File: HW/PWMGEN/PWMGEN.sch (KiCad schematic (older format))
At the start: 28 parts, among them Q1 MMBT3904, U2 MCP1825ST-3302E/DB, U3 uA78M05C, U4 STM32L011D4Px, U5 LM4132AMF-3.3

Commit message: updated layout
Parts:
- R7: footprint Resistor_SMD:R_1206_3216Metric_Pad1.42x1.75mm_HandSolder -> Resistor_THT:R_Axial_DIN0207_L6.3mm_D2.5mm_P7.62mm_Horizontal
- U2, U3: symbol Regulator_Linear:LM78M05_TO220 -> PWMGEN-rescue:LM78M05_TO220-Regulator_Linear
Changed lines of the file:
@@
 	7600 3650 7600 3850
 $Comp
-L Regulator_Linear:LM78M05_TO220 U2
+L PWMGEN-rescue:LM78M05_TO220-Regulator_Linear U2
 U 1 1 5D9A22DE
 P 4300 1750
@@
 $EndComp
 $Comp
-L Regulator_Linear:LM78M05_TO220 U3
+L PWMGEN-rescue:LM78M05_TO220-Regulator_Linear U3
 U 1 1 5D9A33C6
 P 2800 1750
@@
 F 0 "R7" V 3850 6150 50  0000 L CNN
 F 1 "5K6" V 4050 6150 50  0000 L CNN
-F 2 "Resistor_SMD:R_1206_3216Metric_Pad1.42x1.75mm_HandSolder" V 3880 6200 50  0001 C CNN
+F 2 "Resistor_THT:R_Axial_DIN0207_L6.3mm_D2.5mm_P7.62mm_Horizontal" V 3880 6200 50  0001 C CNN
 F 3 "~" H 3950 6200 50  0001 C CNN
 	1    3950 6200

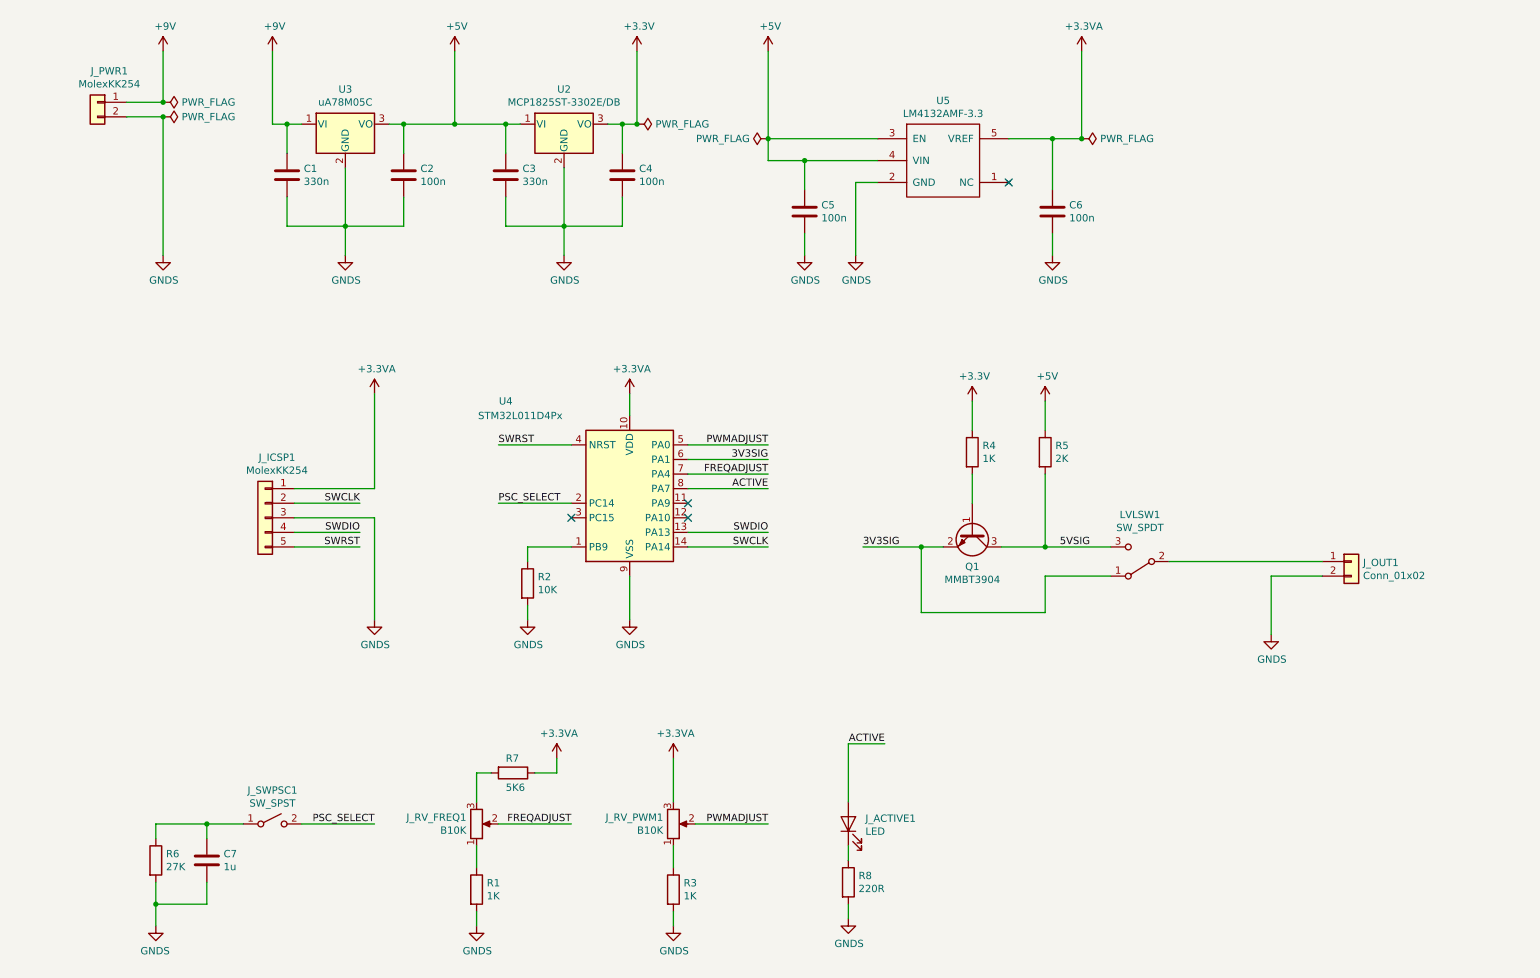
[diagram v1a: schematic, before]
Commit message: updated MCU, layout, sw
- Changed from STM32L011D4 to STM32F051K8
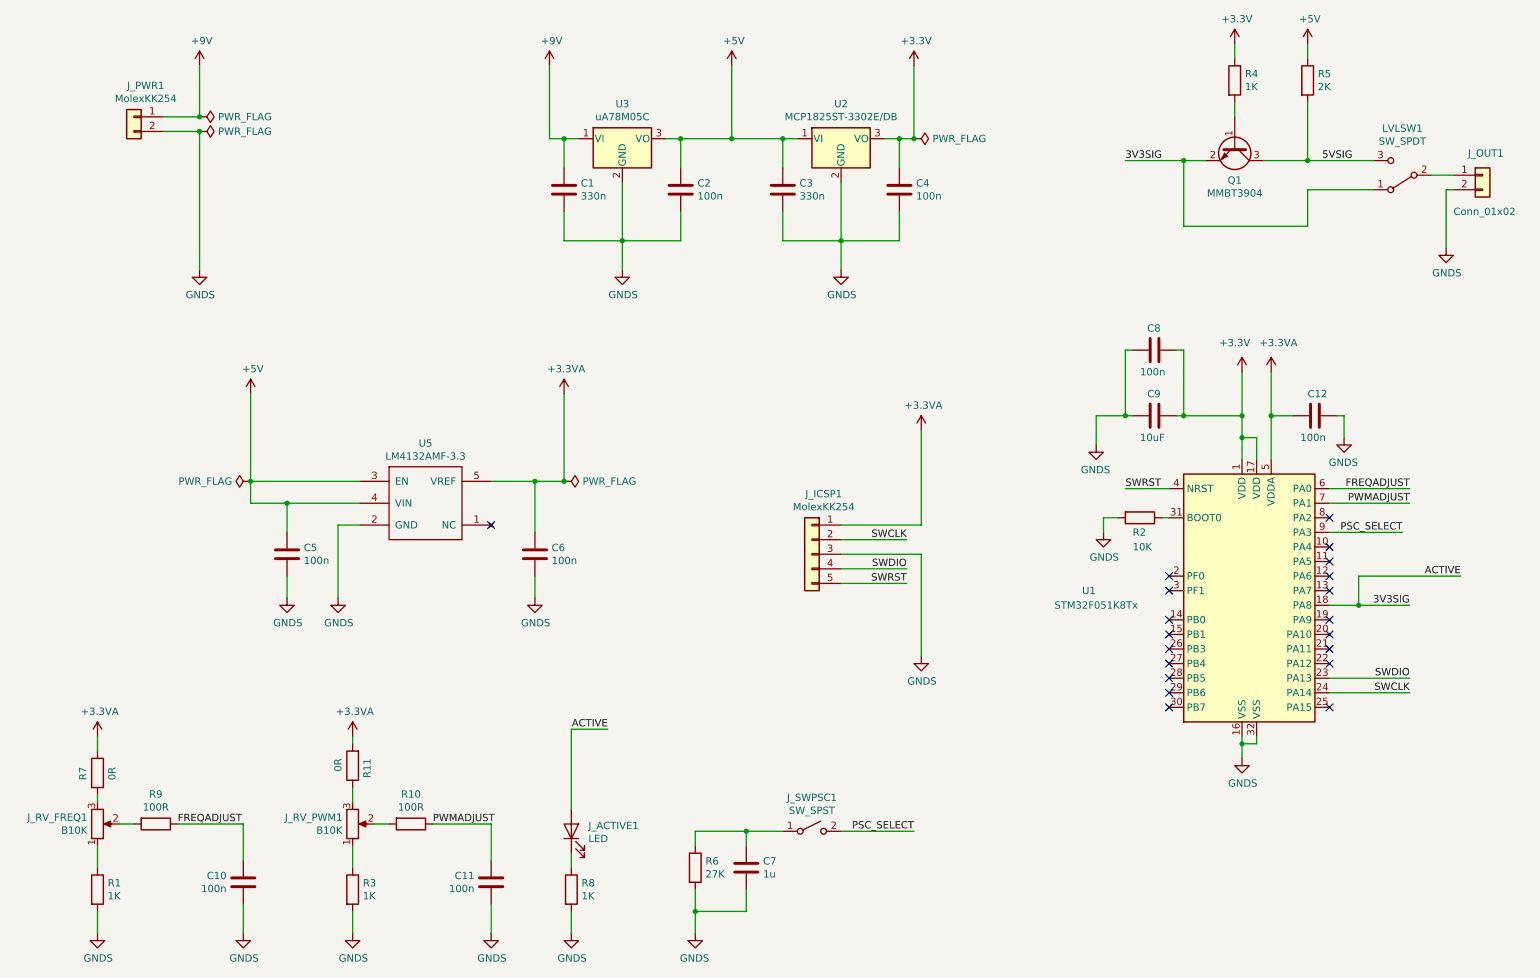
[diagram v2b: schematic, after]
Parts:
- removed U4: STM32L011D4Px, Package_SO:TSSOP-14_4.4x5mm_P0.65mm, symbol MCU_ST_STM32L0:STM32L011D4Px
- added C10, C11, C12, C8: 100n, Capacitor_SMD:C_1206_3216Metric_Pad1.42x1.75mm_HandSolder, symbol Device:C
- added C9: 10uF, Capacitor_SMD:C_1206_3216Metric_Pad1.42x1.75mm_HandSolder, symbol Device:C
- added R10, R9: 100R, Resistor_SMD:R_1206_3216Metric_Pad1.42x1.75mm_HandSolder, symbol Device:R
- added R11: 0R, Resistor_SMD:R_1206_3216Metric_Pad1.42x1.75mm_HandSolder, symbol Device:R
- added U1: STM32F051K8Tx, Package_QFP:LQFP-32_7x7mm_P0.8mm, symbol MCU_ST_STM32F0:STM32F051K8Tx
- J_SWPSC1: footprint Connector_PinHeader_2.54mm:PinHeader_1x03_P2.54mm_Vertical -> Connector_PinHeader_2.54mm:PinHeader_1x02_P2.54mm_Vertical
- R7: value 5K6 -> 0R; footprint Resistor_THT:R_Axial_DIN0207_L6.3mm_D2.5mm_P7.62mm_Horizontal -> Resistor_SMD:R_1206_3216Metric_Pad1.42x1.75mm_HandSolder
- R8: value 220R -> 1K
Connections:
- net ACTIVE is gone; now on net 3V3SIG: J_ACTIVE1.2 (A)
- net +3.3VA: now also C12.2, R11.2, U1.5 (VDDA); no longer J_RV_PWM1.3
- net +3V3: now also C8.1, C9.1, U1.1 (VDD), U1.17 (VDD)
- net 3V3SIG: now also U1.18 (PA8)
- net FREQADJUST: now also C10.1, R9.1, U1.6 (PA0); no longer J_RV_FREQ1.2
- net GNDS: now also C10.2, C11.2, C12.1, C8.2, C9.2, U1.16 (VSS), U1.32 (VSS)
- net PSC_SELECT: now also U1.9 (PA3)
- net PWMADJUST: now also C11.1, R10.1, U1.7 (PA1); no longer J_RV_PWM1.2
- net SWCLK: now also U1.24 (PA14)
- net SWDIO: now also U1.23 (PA13)
- net SWRST: now also U1.4 (NRST)
- net at R2.1: now also U1.31 (BOOT0)
- new net: J_RV_PWM1.2, R10.2
- new net: J_RV_PWM1.3, R11.1
- new net: J_RV_FREQ1.2, R9.2
- no-connect marks 4 -> 20
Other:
- moved on the sheet: C1, C2, C3, C4, C5, C6, C7, J_ACTIVE1, J_ICSP1, J_OUT1, J_PWR1, J_RV_FREQ1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

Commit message: UPDATES
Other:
- note added: "CURRENT\nLIMITER"
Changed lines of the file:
@@
 Wire Wire Line
 	1100 6350 1100 6400
+Text Notes 700  7050 0    50   ~ 0
+CURRENT\nLIMITER
 $EndSCHEMATC

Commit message: UPDATES
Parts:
- removed C10, C11: 100n, Capacitor_SMD:C_1206_3216Metric_Pad1.42x1.75mm_HandSolder, symbol Device:C
- removed R10: 100R, Resistor_SMD:R_1206_3216Metric_Pad1.42x1.75mm_HandSolder, symbol Device:R
- R1: value 1K -> 2k
- R3: value 1K -> 0R
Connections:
- net FREQADJUST: now also J_RV_FREQ1.2; no longer R9.1
- net PWMADJUST: now also J_RV_PWM1.2
- net at R9.2: now also LVLSW1.2 (B); no longer J_RV_FREQ1.2
- net at J_OUT1.1 (Pin_1): now also R9.1; no longer LVLSW1.2 (B)
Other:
- moved on the sheet: LVLSW1, Q1, R4, R5
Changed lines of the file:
@@
 P 2850 7000
 F 0 "R3" H 2920 7045 50  0000 L CNN
-F 1 "1K" H 2920 6956 50  0000 L CNN
+F 1 "0R" H 2920 6956 50  0000 L CNN
 F 2 "Resistor_SMD:R_1206_3216Metric_Pad1.42x1.75mm_HandSolder" V 2780 7000 50  0001 C CNN
 F 3 "~" H 2850 7000 50  0001 C CNN
@@
 	1    0    0    -1
 $EndComp
-Text Label 3400 6550 0    50   ~ 0
+Text Label 3550 6550 2    50   ~ 0
 PWMADJUST
 $Comp
@@
 P 1100 7000
 F 0 "R1" H 1170 7045 50  0000 L CNN
-F 1 "1K" H 1170 6956 50  0000 L CNN
+F 1 "2k" H 1170 6956 50  0000 L CNN
 F 2 "Resistor_SMD:R_1206_3216Metric_Pad1.42x1.75mm_HandSolder" V 1030 7000 50  0001 C CNN
 F 3 "~" H 1100 7000 50  0001 C CNN
@@
 	1    0    0    -1
 $EndComp
-Wire Wire Line
-	1250 6550 1350 6550
-Text Label 1650 6550 0    50   ~ 0
+Text Label 1800 6550 2    50   ~ 0
 FREQADJUST
 Wire Wire Line
@@
 L Transistor_BJT:MMBT3904 Q1
 U 1 1 5D98DE38
-P 8900 1900
-F 0 "Q1" V 9135 1900 50  0000 C CNN
-F 1 "MMBT3904" V 9224 1900 50  0000 C CNN
-F 2 "Package_TO_SOT_SMD:SOT-23" H 9100 1825 50  0001 L CIN
-F 3 "https://docs-emea.rs-online.com/webdocs/1276/0900766b81276adc.pdf" H 8900 1900 50  0001 L CNN
-	1    8900 1900
+P 8550 1900
+F 0 "Q1" V 8785 1900 50  0000 C CNN
+F 1 "MMBT3904" V 8874 1900 50  0000 C CNN
+F 2 "Package_TO_SOT_SMD:SOT-23" H 8750 1825 50  0001 L CIN
+F 3 "https://docs-emea.rs-online.com/webdocs/1276/0900766b81276adc.pdf" H 8550 1900 50  0001 L CNN
+	1    8550 1900
 	0    1    1    0
 $EndComp
@@
 L Device:R R4
 U 1 1 5D98FAB4
-P 8900 1450
-F 0 "R4" H 8970 1495 50  0000 L CNN
-F 1 "1K" H 8970 1406 50  0000 L CNN
-F 2 "Resistor_SMD:R_1206_3216Metric_Pad1.42x1.75mm_HandSolder" V 8830 1450 50  0001 C CNN
-F 3 "~" H 8900 1450 50  0001 C CNN
-	1    8900 1450
+P 8550 1450
+F 0 "R4" H 8620 1495 50  0000 L CNN
+F 1 "1K" H 8620 1406 50  0000 L CNN
+F 2 "Resistor_SMD:R_1206_3216Metric_Pad1.42x1.75mm_HandSolder" V 8480 1450 50  0001 C CNN
+F 3 "~" H 8550 1450 50  0001 C CNN
+	1    8550 1450
 	1    0    0    -1
 $EndComp
@@
 L Device:R R5
 U 1 1 5D98FCF4
-P 9400 1450
-F 0 "R5" H 9470 1495 50  0000 L CNN
-F 1 "2K" H 9470 1406 50  0000 L CNN
-F 2 "Resistor_SMD:R_1206_3216Metric_Pad1.42x1.75mm_HandSolder" V 9330 1450 50  0001 C CNN
-F 3 "~" H 9400 1450 50  0001 C CNN
-	1    9400 1450
-	1    0    0    -1
-$EndComp
-Wire Wire Line
-	9100 2000 9400 2000
-Wire Wire Line
-	9400 2000 9400 1600
-Wire Wire Line
-	8900 1600 8900 1700
-Wire Wire Line
-	8700 2000 8550 2000
-Text Label 8150 2000 0    50   ~ 0
+P 9050 1450
+F 0 "R5" H 9120 1495 50  0000 L CNN
+F 1 "2K" H 9120 1406 50  0000 L CNN
+F 2 "Resistor_SMD:R_1206_3216Metric_Pad1.42x1.75mm_HandSolder" V 8980 1450 50  0001 C CNN
+F 3 "~" H 9050 1450 50  0001 C CNN
+	1    9050 1450
+	1    0    0    -1
+$EndComp
+Wire Wire Line
+	8750 2000 9050 2000
+Wire Wire Line
+	9050 2000 9050 1600
+Wire Wire Line
+	8550 1600 8550 1700
+Wire Wire Line
+	8350 2000 8200 2000
+Text Label 7800 2000 0    50   ~ 0
 3V3SIG
 $Comp
 L power:+3.3V #PWR020
 U 1 1 5D9978E0
-P 8900 1200
-F 0 "#PWR020" H 8900 1050 50  0001 C CNN
-F 1 "+3.3V" H 8915 1371 50  0000 C CNN
-F 2 "" H 8900 1200 50  0001 C CNN
-F 3 "" H 8900 1200 50  0001 C CNN
-	1    8900 1200
-	1    0    0    -1
-$EndComp
-Wire Wire Line
-	8900 1200 8900 1300
+P 8550 1200
+F 0 "#PWR020" H 8550 1050 50  0001 C CNN
+F 1 "+3.3V" H 8565 1371 50  0000 C CNN
+F 2 "" H 8550 1200 50  0001 C CNN
+F 3 "" H 8550 1200 50  0001 C CNN
+	1    8550 1200
+	1    0    0    -1
+$EndComp
+Wire Wire Line
+	8550 1200 8550 1300
 $Comp
 L power:+5V #PWR022
 U 1 1 5D998A8A
-P 9400 1200
-F 0 "#PWR022" H 9400 1050 50  0001 C CNN
-F 1 "+5V" H 9415 1371 50  0000 C CNN
-F 2 "" H 9400 1200 50  0001 C CNN
-F 3 "" H 9400 1200 50  0001 C CNN
-	1    9400 1200
-	1    0    0    -1
-$EndComp
-Wire Wire Line
-	9400 1200 9400 1300
+P 9050 1200
+F 0 "#PWR022" H 9050 1050 50  0001 C CNN
+F 1 "+5V" H 9065 1371 50  0000 C CNN
+F 2 "" H 9050 1200 50  0001 C CNN
+F 3 "" H 9050 1200 50  0001 C CNN
+	1    9050 1200
+	1    0    0    -1
+$EndComp
+Wire Wire Line
+	9050 1200 9050 1300
 $Comp
 L PWMGEN-rescue:LM78M05_TO220-Regulator_Linear U2
@@
 L Switch:SW_SPDT LVLSW1
 U 1 1 5DA00401
-P 10050 2100
-F 0 "LVLSW1" H 10050 1779 50  0000 C CNN
-F 1 "SW_SPDT" H 10050 1868 50  0000 C CNN
-F 2 "Connector_PinHeader_2.54mm:PinHeader_1x03_P2.54mm_Vertical" H 10050 2100 50  0001 C CNN
-F 3 "~" H 10050 2100 50  0001 C CNN
-	1    10050 2100
+P 9700 2100
+F 0 "LVLSW1" H 9700 1779 50  0000 C CNN
+F 1 "SW_SPDT" H 9700 1868 50  0000 C CNN
+F 2 "Connector_PinHeader_2.54mm:PinHeader_1x03_P2.54mm_Vertical" H 9700 2100 50  0001 C CNN
+F 3 "~" H 9700 2100 50  0001 C CNN
+	1    9700 2100
 	-1   0    0    1
 $EndComp
 Text Label 10100 5050 2    50   ~ 0
 3V3SIG
-Text Label 9500 2000 0    50   ~ 0
+Text Label 9150 2000 0    50   ~ 0
 5VSIG
 Wire Wire Line
-	9400 2000 9850 2000
-Connection ~ 9400 2000
-Wire Wire Line
-	9850 2200 9400 2200
-Wire Wire Line
-	9400 2200 9400 2450
-Wire Wire Line
-	9400 2450 8550 2450
-Wire Wire Line
-	8550 2450 8550 2000
-Connection ~ 8550 2000
-Wire Wire Line
-	8550 2000 8150 2000
-Wire Wire Line
-	10250 2100 10400 2100
+	9050 2000 9500 2000
+Connection ~ 9050 2000
+Wire Wire Line
+	9500 2200 9050 2200
+Wire Wire Line
+	9050 2200 9050 2450
+Wire Wire Line
+	9050 2450 8200 2450
+Wire Wire Line
+	8200 2450 8200 2000
+Connection ~ 8200 2000
+Wire Wire Line
+	8200 2000 7800 2000
+Wire Wire Line
+	9900 2100 10000 2100
 $Comp
 L Switch:SW_SPST J_SWPSC1
@@
 Wire Wire Line
 	8150 3300 8150 3750
-$Comp
-L Device:R R9
-U 1 1 5DB76795
-P 1500 6550
-F 0 "R9" V 1296 6550 50  0000 C CNN
-F 1 "100R" V 1385 6550 50  0000 C CNN
-F 2 "Resistor_SMD:R_1206_3216Metric_Pad1.42x1.75mm_HandSolder" V 1430 6550 50  0001 C CNN
-F 3 "~" H 1500 6550 50  0001 C CNN
-	1    1500 6550
-	0    1    1    0
-$EndComp
-Wire Wire Line
-	1650 6550 2100 6550
-Wire Wire Line
-	2100 6550 2100 6800
-$Comp
-L Device:C C10
-U 1 1 5DB84409
-P 2100 6950
-F 0 "C10" H 2215 6995 50  0000 L CNN
-F 1 "100n" H 2215 6906 50  0000 L CNN
-F 2 "Capacitor_SMD:C_1206_3216Metric_Pad1.42x1.75mm_HandSolder" H 2138 6800 50  0001 C CNN
-F 3 "~" H 2100 6950 50  0001 C CNN
-	1    2100 6950
-	-1   0    0    -1
-$EndComp
-Wire Wire Line
-	2100 7100 2100 7300
-$Comp
-L power:GNDS #PWR026
-U 1 1 5DB84D0A
-P 2100 7300
-F 0 "#PWR026" H 2100 7050 50  0001 C CNN
-F 1 "GNDS" H 2105 7129 50  0000 C CNN
-F 2 "" H 2100 7300 50  0001 C CNN
-F 3 "" H 2100 7300 50  0001 C CNN
-	1    2100 7300
-	1    0    0    -1
-$EndComp
-Wire Wire Line
-	3000 6550 3100 6550
-$Comp
-L Device:R R10
-U 1 1 5DB8EF07
-P 3250 6550
-F 0 "R10" V 3046 6550 50  0000 C CNN
-F 1 "100R" V 3135 6550 50  0000 C CNN
-F 2 "Resistor_SMD:R_1206_3216Metric_Pad1.42x1.75mm_HandSolder" V 3180 6550 50  0001 C CNN
-F 3 "~" H 3250 6550 50  0001 C CNN
-	1    3250 6550
-	0    1    1    0
-$EndComp
-Wire Wire Line
-	3400 6550 3800 6550
-Wire Wire Line
-	3800 6550 3800 6800
-$Comp
-L Device:C C11
-U 1 1 5DB8EF0F
-P 3800 6950
-F 0 "C11" H 3915 6995 50  0000 L CNN
-F 1 "100n" H 3915 6906 50  0000 L CNN
-F 2 "Capacitor_SMD:C_1206_3216Metric_Pad1.42x1.75mm_HandSolder" H 3838 6800 50  0001 C CNN
-F 3 "~" H 3800 6950 50  0001 C CNN
-	1    3800 6950
-	-1   0    0    -1
-$EndComp
-Wire Wire Line
-	3800 7100 3800 7300
-$Comp
-L power:GNDS #PWR027
-U 1 1 5DB8EF16
-P 3800 7300
-F 0 "#PWR027" H 3800 7050 50  0001 C CNN
-F 1 "GNDS" H 3805 7129 50  0000 C CNN
-F 2 "" H 3800 7300 50  0001 C CNN
-F 3 "" H 3800 7300 50  0001 C CNN
-	1    3800 7300
-	1    0    0    -1
-$EndComp
+Wire Wire Line
+	3000 6550 3550 6550
 Wire Wire Line
 	9650 3750 9600 3750
@@
 Text Notes 700  7050 0    50   ~ 0
 CURRENT\nLIMITER
+Wire Wire Line
+	1250 6550 1800 6550
+$Comp
+L Device:R R9
+U 1 1 5D9EE60A
+P 10150 2100
+F 0 "R9" V 9950 2050 50  0000 L CNN
+F 1 "100R" V 10050 2050 50  0000 L CNN
+F 2 "Resistor_SMD:R_1206_3216Metric_Pad1.42x1.75mm_HandSolder" V 10080 2100 50  0001 C CNN
+F 3 "~" H 10150 2100 50  0001 C CNN
+	1    10150 2100
+	0    1    1    0
+$EndComp
+Wire Wire Line
+	10300 2100 10400 2100
 $EndSCHEMATC

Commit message: update
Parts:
- removed Q1: MMBT3904, Package_TO_SOT_SMD:SOT-23, symbol Transistor_BJT:MMBT3904
- added Q1: PZT2222A, Package_TO_SOT_SMD:SOT-223, symbol Transistor_BJT:PZT2222A
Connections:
- net 3V3SIG: now also Q1.3 (E)
- net 5VSIG: now also Q1.2 (C)
- net at R4.2: now also Q1.1 (B)
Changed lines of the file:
@@
-$EndComp
-$Comp
-L Transistor_BJT:MMBT3904 Q1
-U 1 1 5D98DE38
-P 8550 1900
-F 0 "Q1" V 8785 1900 50  0000 C CNN
-F 1 "MMBT3904" V 8874 1900 50  0000 C CNN
-F 2 "Package_TO_SOT_SMD:SOT-23" H 8750 1825 50  0001 L CIN
-F 3 "https://docs-emea.rs-online.com/webdocs/1276/0900766b81276adc.pdf" H 8550 1900 50  0001 L CNN
-	1    8550 1900
-	0    1    1    0
 $EndComp
 $Comp
@@
 Wire Wire Line
 	10300 2100 10400 2100
+$Comp
+L Transistor_BJT:PZT2222A Q1
+U 1 1 5D9DF7B8
+P 8550 1900
+F 0 "Q1" V 8785 1900 50  0000 C CNN
+F 1 "PZT2222A" V 8876 1900 50  0000 C CNN
+F 2 "Package_TO_SOT_SMD:SOT-223" H 8750 1825 50  0001 L CIN
+F 3 "http://www.fairchildsemi.com/ds/PN/PN2222A.pdf" H 8550 1900 50  0001 L CNN
+	1    8550 1900
+	0    1    1    0
+$EndComp
 $EndSCHEMATC

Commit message: updates
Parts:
- removed R11, R7: 0R, Resistor_SMD:R_1206_3216Metric_Pad1.42x1.75mm_HandSolder, symbol Device:R
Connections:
- net +3.3VA: now also J_RV_FREQ1.3, J_RV_PWM1.3
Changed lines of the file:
@@
 $EndComp
-Wire Wire Line
-	2850 6400 2850 6300
 Wire Wire Line
 	2850 6700 2850 6850
@@
 Connection ~ 5200 7150
 $Comp
-L Device:R R7
-U 1 1 5DA38252
-P 1100 6200
-F 0 "R7" V 1000 6150 50  0000 L CNN
-F 1 "0R" V 1200 6150 50  0000 L CNN
-F 2 "Resistor_SMD:R_1206_3216Metric_Pad1.42x1.75mm_HandSolder" V 1030 6200 50  0001 C CNN
-F 3 "~" H 1100 6200 50  0001 C CNN
-	1    1100 6200
-	1    0    0    -1
-$EndComp
-$Comp
 L power:PWR_FLAG #FLG0101
 U 1 1 5DA4BE47
@@
 Wire Wire Line
 	4350 5900 4600 5900
-Wire Wire Line
-	1100 6050 1100 5950
 $Comp
 L MCU_ST_STM32F0:STM32F051K8Tx U1
@@
 Wire Wire Line
 	9150 3750 9150 4050
-$Comp
-L Device:R R11
-U 1 1 5DC72B3E
-P 2850 6150
-F 0 "R11" V 2750 6100 50  0000 L CNN
-F 1 "0R" V 2950 6100 50  0000 L CNN
-F 2 "Resistor_SMD:R_1206_3216Metric_Pad1.42x1.75mm_HandSolder" V 2780 6150 50  0001 C CNN
-F 3 "~" H 2850 6150 50  0001 C CNN
-	1    2850 6150
-	-1   0    0    1
-$EndComp
-Wire Wire Line
-	2850 6000 2850 5950
-Wire Wire Line
-	1100 6350 1100 6400
 Text Notes 700  7050 0    50   ~ 0
 CURRENT\nLIMITER
@@
 	0    1    1    0
 $EndComp
+Wire Wire Line
+	2850 5950 2850 6400
+Wire Wire Line
+	1100 5950 1100 6400
 $EndSCHEMATC
